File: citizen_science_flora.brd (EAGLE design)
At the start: 86.6 x 79.6 mm, 90 parts, among them IC1 W25Q64JVXGIQ, J1 SM03B-SRSS-TB(LF)(SN), J2 TYPE-C-31-M-12, J4 60312202114511, J5 60312202114511, U1 RP2350A, U2 APS6404L-3SQR-ZR, U3 ESP32-C3-MINI-1-N4, U4 MIC5504-3.3YM5-T5, U5 BME690, U6 ADM3260ARSZ, U7 ENS210-LQFM, U8 SFH6325-X017TEL0631, U9 AS3935-BQFT, Y1 12MHz

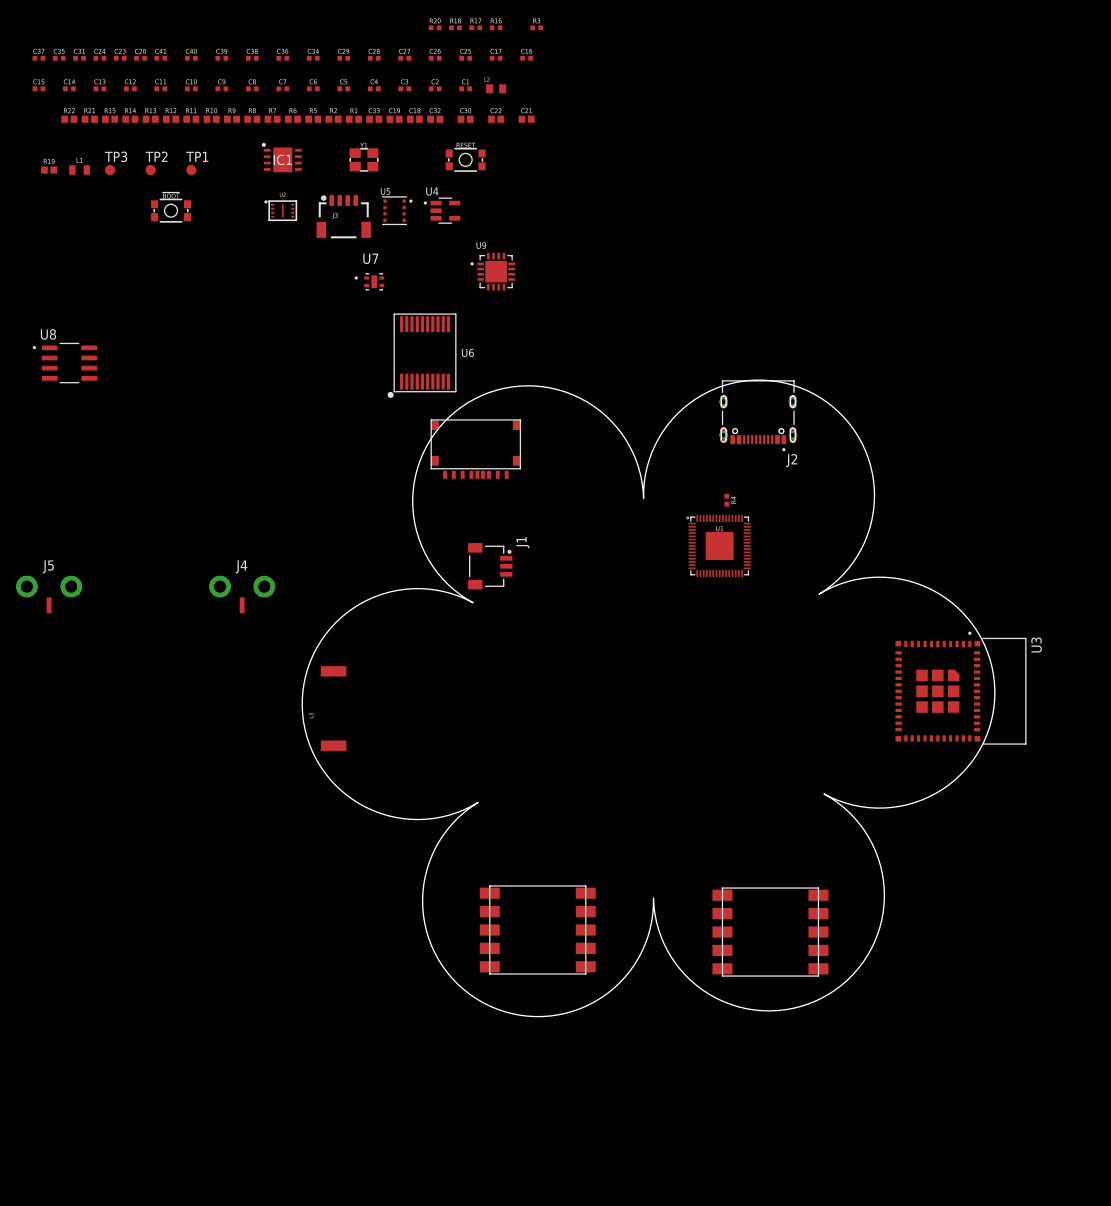
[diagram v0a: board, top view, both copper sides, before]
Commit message: placed some components
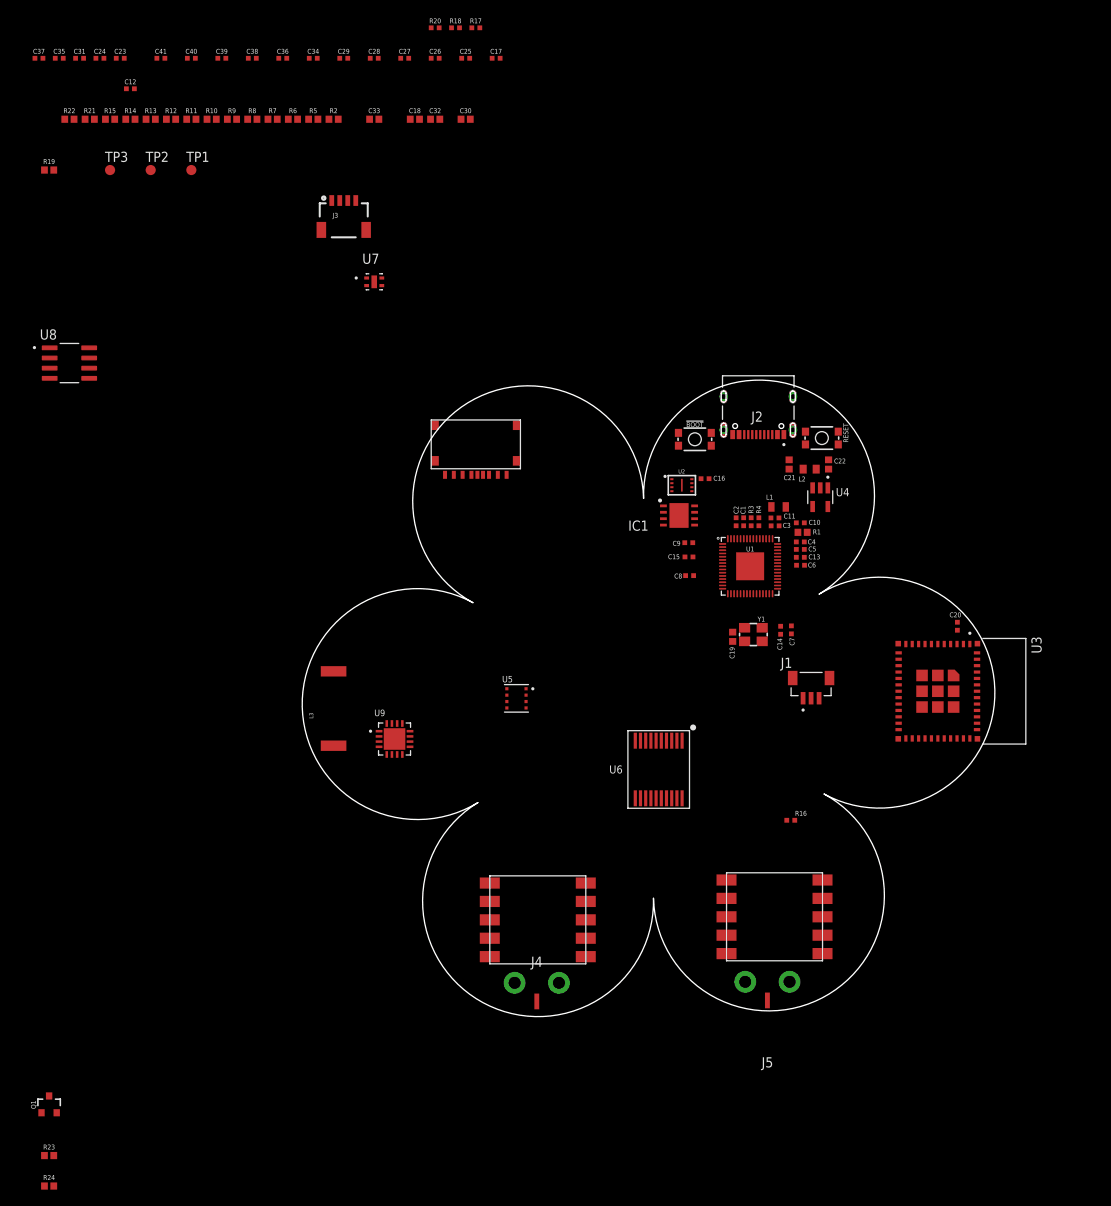
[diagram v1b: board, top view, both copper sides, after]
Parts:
- added Q1: 220mA/50V/3.5Ω, SparkFun-DiscreteSemi:SOT23-3
- added R23, R24: 1M, SparkFun-Resistors:0402
- J1: value SM03B-SRSS-TB(LF)(SN) -> BM03B-SRSS-TB(LF)(SN); device SM03B-SRSS-TB_LF__SN_:JST_SM03B-SRSS-TB(LF)(SN) -> BM03B-SRSS-TB_LF__SN_:JST_BM03B-SRSS-TB(LF)(SN)
- R12: value 10K -> 2.2K
- moved C20 124.4 mm to (38.6, 9.02), turned to 90 degrees
- moved C14 111.7 mm to (16.5, 8.51), turned to 270 degrees
- moved R16 105.7 mm to (17.8, -15.2)
- moved C13 105.3 mm to (19.0, 17.6)
- moved J5 102.5 mm to (14.9, -35.4)
- moved C15 100.1 mm to (5.05, 17.7), turned to 180 degrees
- moved L1 97.0 mm to (16.3, 23.9), turned to 180 degrees
- moved C11 93.6 mm to (15.8, 22.6)
- moved C10 93.5 mm to (19.0, 21.9)
- moved C7 92.8 mm to (17.9, 8.56), turned to 270 degrees
- moved C6 85.2 mm to (19.0, 16.6)
- moved C8 81.8 mm to (5.13, 15.3), turned to 180 degrees
- moved C9 81.4 mm to (5.03, 19.5), turned to 180 degrees
- moved C5 81.1 mm to (19.0, 18.6)
- moved C4 77.8 mm to (19.0, 19.6)
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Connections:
- new net PDIS_EN: Q1.1, R24.1, U1.12
- net 3.3V: now also R24.2
- net GND: now also Q1.2
- net PDIS: now also Q1.3, R23.1; no longer U1.12
- net V_USB: now also R23.2

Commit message: Add 3D packages to resistors
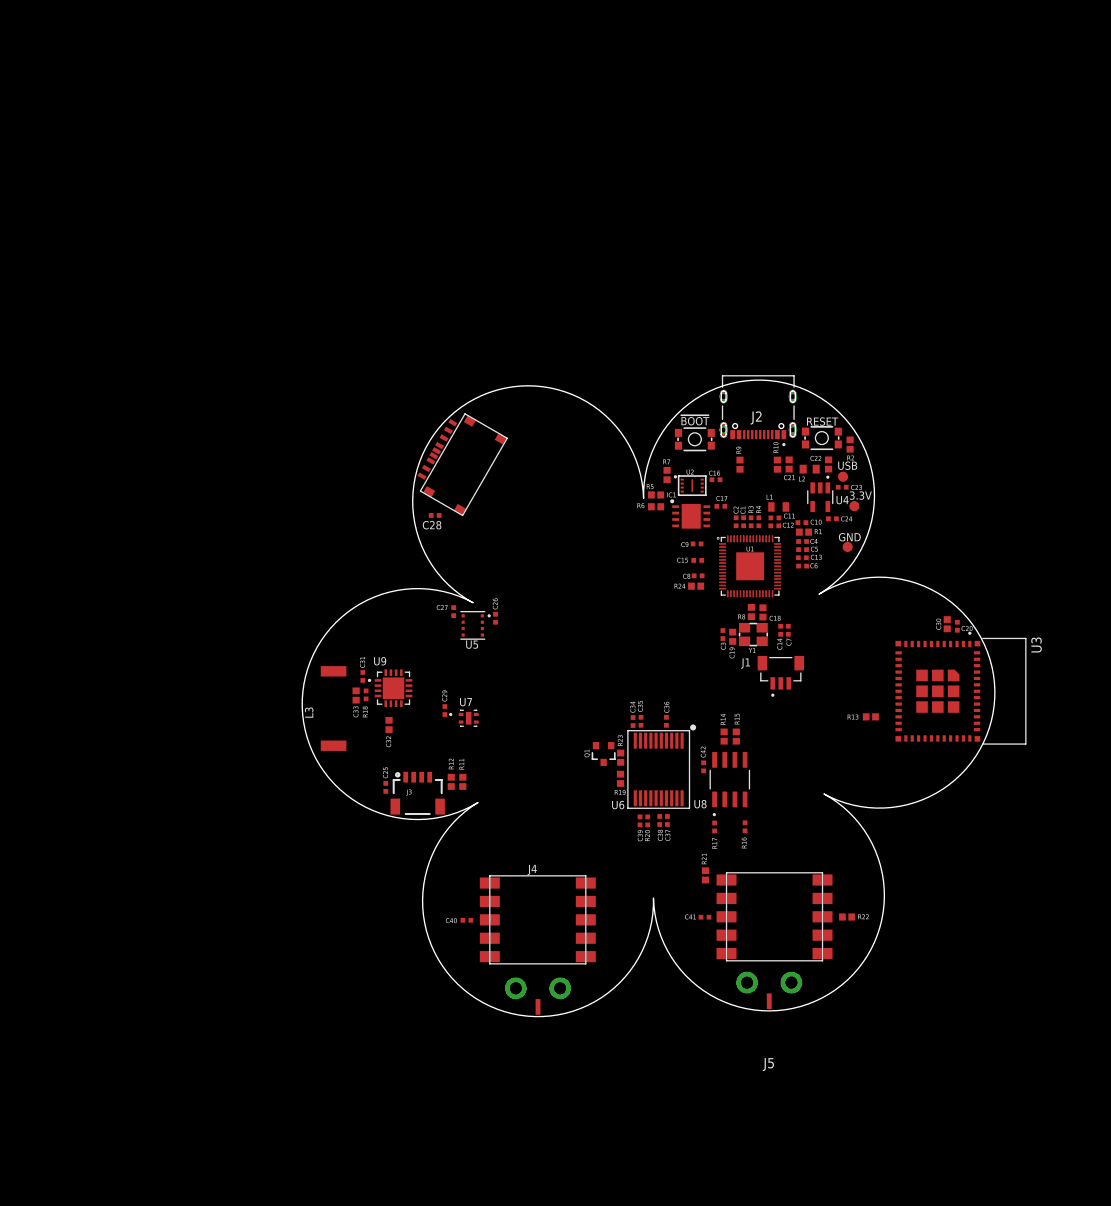
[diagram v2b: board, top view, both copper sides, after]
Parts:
- removed TP1, TP2, TP3: TPB1,27, testpad:B1,27
- added 3.3V, GND: TPB1,27, testpad:B1,27
- added C42: 0.1uF, SparkFun-Capacitors:0402-TIGHT
- added USB: V_USB, testpad:B1,27
- moved R22 139.3 mm to (24.8, -27.3)
- moved C41 127.1 mm to (7.06, -27.4)
- moved C37 123.5 mm to (2.36, -15.3), turned to 270 degrees
- moved R21 121.9 mm to (7.11, -22.1), turned to 90 degrees
- moved R13 117.0 mm to (27.8, -2.31), turned to 180 degrees
- moved C40 113.1 mm to (-22.7, -27.7)
- moved R24 110.3 mm to (5.94, 14.0), turned to 180 degrees
- moved C35 110.3 mm to (-0.94, -2.87), turned to 270 degrees
- moved R15 109.9 mm to (11.0, -4.78), turned to 90 degrees
- moved C39 108.7 mm to (-1.07, -15.3), turned to 270 degrees
- moved C24 108.2 mm to (23.0, 22.5), turned to 180 degrees
- moved C38 108.0 mm to (1.40, -15.3), turned to 270 degrees
- moved R14 107.1 mm to (9.45, -4.78), turned to 90 degrees
- moved C23 105.0 mm to (24.2, 26.4), turned to 180 degrees
- moved R19 104.4 mm to (-3.51, -10.1), turned to 270 degrees
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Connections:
- net 3.3V: now also 3.3V.TP, C42.2; no longer TP3.TP
- net GND: now also C42.1, GND.TP; no longer TP2.TP
- net V_USB: now also USB.TP; no longer TP1.TP

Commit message: Board file updates
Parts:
- added C43: RSCSK2043R3D01004T, SamacSys_Parts:RSCSK2043R3D01004T
- added C44, C45, C46, C49, C50, C51, C52: 0.1uF, SparkFun-Capacitors:0402
- added C47, C48: 12pF, SparkFun-Capacitors:0402
- added D1: 1N4148, SparkFun-DiscreteSemi:SOD-323
- added D2: 1N5819, SparkFun-DiscreteSemi:SOD-323
- added J6: TSM-102-02-S-SH, TSM-102-02-S-SH:SAMTEC_TSM-102-02-S-SH
- added LS1: MLT-8530, CMT-8504-100-SMT-TR:XDCR_CMT-8504-100-SMT-TR
- added Q2: BSS138, SparkFun-DiscreteSemi:SOT323
- added R25: 470, SparkFun-Resistors:0402
- added U10: PCF8563T/F4,118, PCF8563T_F4_118:SOIC127P600X175-8N
- added U11, U12, U13, U14: OPS-S56AAF5, OPS=S56AAF5:OPS-S56AAF5
- added U15: SN74LVC1T45DBVRG4, SN74LVC1T45DBVRG4:SOT95P280X145-6N
- added USR_BUTTON: MOMENTARY-SWITCH-SPST-SMD-4.6X2.8MM, SparkFun-Switches:TACTILE_SWITCH_SMD_4.6X2.8MM
- added XTAL1: Q13FC1350000400, Q13FC1350000400:XTAL_FC-135_EPS
- J1: value BM03B-SRSS-TB(LF)(SN) -> SM03B-SRSS-TB(LF)(SN); device BM03B-SRSS-TB_LF__SN_:JST_BM03B-SRSS-TB(LF)(SN) -> SM03B-SRSS-TB_LF__SN_:JST_SM03B-SRSS-TB(LF)(SN)
- moved R14 14.7 mm to (18.6, -16.3), turned to 0 degrees
- moved J1 13.2 mm to (28.6, 9.78), turned to 180 degrees
- moved R15 12.6 mm to (18.6, -14.9), turned to 0 degrees
- moved U7 11.2 mm to (-26.4, 8.00)
- moved C29 11.0 mm to (-30.0, 8.46), turned to 180 degrees
- moved C34 10.8 mm to (-2.87, -13.6), turned to 0 degrees
- moved Q1 10.7 mm to (-8.59, -17.2), turned to 270 degrees
- moved C27 10.4 mm to (-28.7, 1.35)
- moved C36 10.2 mm to (0.97, -13.0)
- moved U6 10.2 mm to (0.00, -19.1)
- moved C35 10.0 mm to (-2.87, -12.7), turned to 0 degrees
- moved R23 9.90 mm to (-5.31, -17.1), turned to 0 degrees
- moved R19 9.86 mm to (-5.26, -19.8), turned to 180 degrees
- moved C26 9.16 mm to (-25.7, 3.63), turned to 0 degrees
- moved U5 9.05 mm to (-26.4, 1.24)
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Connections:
- new net BUZZER_DRIVER: R25.2, U1.9
- new net INT_RTC: U1.40, U10.3
- new net N$22: U11.P$2, U12.P$4
- new net N$23: U12.P$2, U13.P$4
- new net N$24: U13.P$2, U14.P$4
- new net N$25: U1.5, USR_BUTTON.1, USR_BUTTON.2
- new net N$26: D1.A, LS1.N, Q2.3
- new net N$27: Q2.1, R25.1
- new net N$28: C43.1, C46.1, D2.C, U10.8
- new net N$29: C48.2, U10.2, XTAL1.1
- new net N$30: C47.2, U10.1, XTAL1.2
- new net NEOPIXEL_3.3V: U1.27, U15.3
- new net NEOPIXEL_5V: U11.P$4, U15.4
- net 3.3V: now also C44.2, D1.C, D2.A, LS1.P, U15.1, U15.5
- net GND: now also C43.2, C44.1, C45.2, C46.2, C47.1, C48.1, C49.2, C50.2, C51.2, C52.2, Q2.2, U10.4, U11.P$3, U12.P$3, U13.P$3, U14.P$3, U15.2, USR_BUTTON.3, USR_BUTTON.4
- net SCL: now also U10.6
- net SDA: now also U10.5
- net V_USB: now also C45.1, C49.1, C50.1, C51.1, C52.1, U11.P$1, U12.P$1, U13.P$1, U14.P$1, U15.6
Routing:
- added copper zone on layer 1, net GND
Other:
- board text added: "BME690"
- board text added: "Capacitor"
- board text added: "I2C Isolator"
- board text added: "Lightning sensor"
- board text added: "MicroSD card"
- board text added: "Platform"
- board text added: "Purple Daisy"
- board text added: "Purple Daisy STEAM platform"
- board text added: "Qwiic"
- board text added: "RP2350A"
- board text added: "RTC"
- board text added: "STEAM"
- board text added: "Soil Temp Sensor"
- board text added: "Soil pH Sensor"
- board text added: "Super"
- board text added: "Temp/Humidity"
- board text added: "Wi-Fi/BLE"

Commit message: Updates to the design
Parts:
- moved R24 0.69 mm to (6.17, 16.7)
- moved C8 0.66 mm to (6.43, 17.9)
- moved R5 0.56 mm to (1.04, 26.8)
- moved R6 0.41 mm to (1.04, 25.2)
- moved C15 0.33 mm to (6.40, 19.8)
- moved C13 0.15 mm to (19.3, 17.7)
- moved C5 0.08 mm to (19.3, 18.7)
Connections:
- net N$18 renamed PRB1
- net N$19 renamed PRB1_GND
- net N$20 renamed PROBE2_GND
- net N$21 renamed PROBE2
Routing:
- net 3.3V: track 0.00 -> 73.6 mm, vias 0 -> 13
- net 1.1V: track 0.00 -> 30.4 mm, vias 0 -> 4
- net SIO2: track 0.00 -> 22.4 mm, vias 0 -> 3
- net SIO1: track 0.00 -> 22.2 mm, vias 0 -> 2
- net !QSPI_CS: track 0.00 -> 16.9 mm
- net SIO3: track 0.00 -> 13.0 mm, vias 0 -> 2
- net SIO0: track 0.00 -> 11.0 mm, vias 0 -> 2
- net USB_P: track 0.00 -> 10.2 mm
- net N$28: track 0.00 -> 10.2 mm
- net N$11: track 0.00 -> 10.1 mm
- net V_USB: track 0.00 -> 9.24 mm
- net USB_N: track 0.00 -> 8.62 mm
- net QSPI_CLK: track 0.00 -> 6.92 mm, vias 0 -> 1
- net N$3: track 0.00 -> 6.61 mm
- net N$2: track 0.00 -> 5.96 mm
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- added copper zone on layer 16, net GND
- added copper zone on layer 2, net GND
- added copper zone on layer 1, net GND-ISO
- added copper zone on layer 16, net GND-ISO
- added copper zone on layer 2, net GND-ISO
- added copper zone on layer 1, net PRB1_GND
- added copper zone on layer 16, net PRB1_GND
- added copper zone on layer 2, net PRB1_GND
- added copper zone on layer 1, net PROBE2_GND
- added copper zone on layer 16, net PROBE2_GND
- added copper zone on layer 2, net PROBE2_GND
- added copper zone on layer 15, net VCC-ISO
